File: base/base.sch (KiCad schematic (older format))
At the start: 24 parts, among them J1 FTDI, J2 Barrel_Jack, J3 CONN_01X40, SW1 SW_Push, U1 Z80CPU, U2 27C256, U3 7404, U4 55257, U5 7432, U6 16550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

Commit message: Cleaned up layout
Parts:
- added SW2: POWER, Buttons_Switches_THT:SW_Tactile_SPST_Angled_PTS645Vx31-2LFS, symbol SW_Push
- added unit 4 of U5
- SW1: value SW_Push -> RESET
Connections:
- net +5V: now also C1.1, U5.14 (Vcc); no longer C1.2
- net GND: now also C1.2, U5.7 (Gnd); no longer C1.1
- net IORQ: now also U5.12; no longer U5.9
- net RESET: no longer J3.20 (P20)
- net UART_CE: now also U5.11; no longer U5.8
- net ~RESET~: now also J3.20 (P20)
- net at U5.10: no longer U3.8
- new net: U3.8, U5.13
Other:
- moved on the sheet: C2, C4, J1, J2, U5C, U7

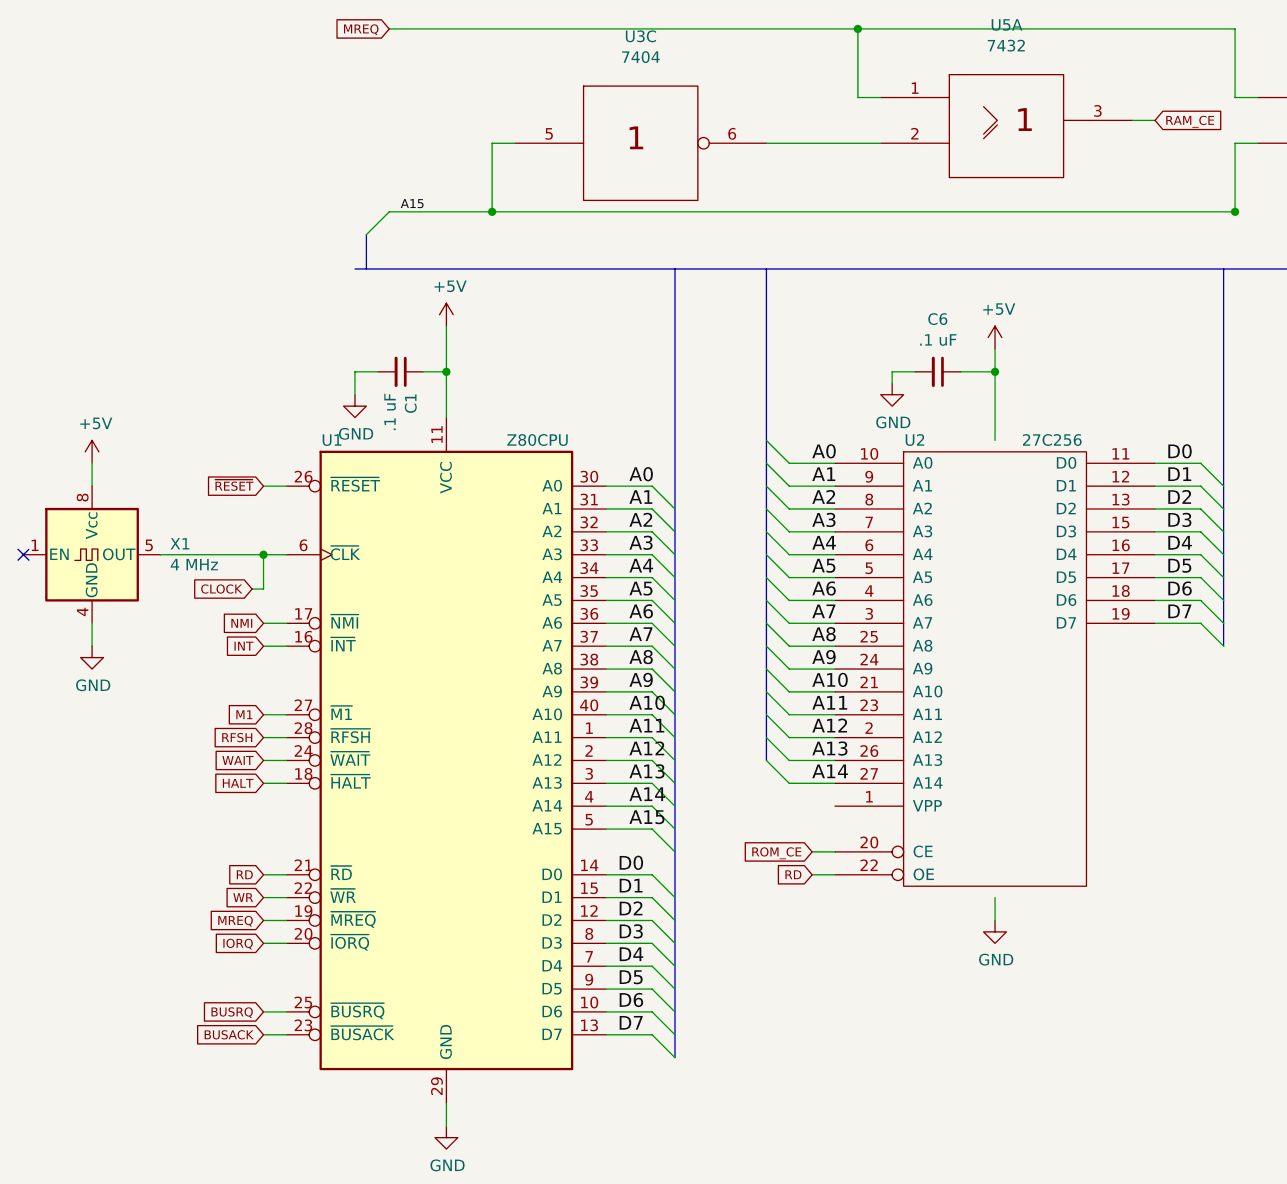
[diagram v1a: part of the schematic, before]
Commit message: Added pullups to busrq and int pins
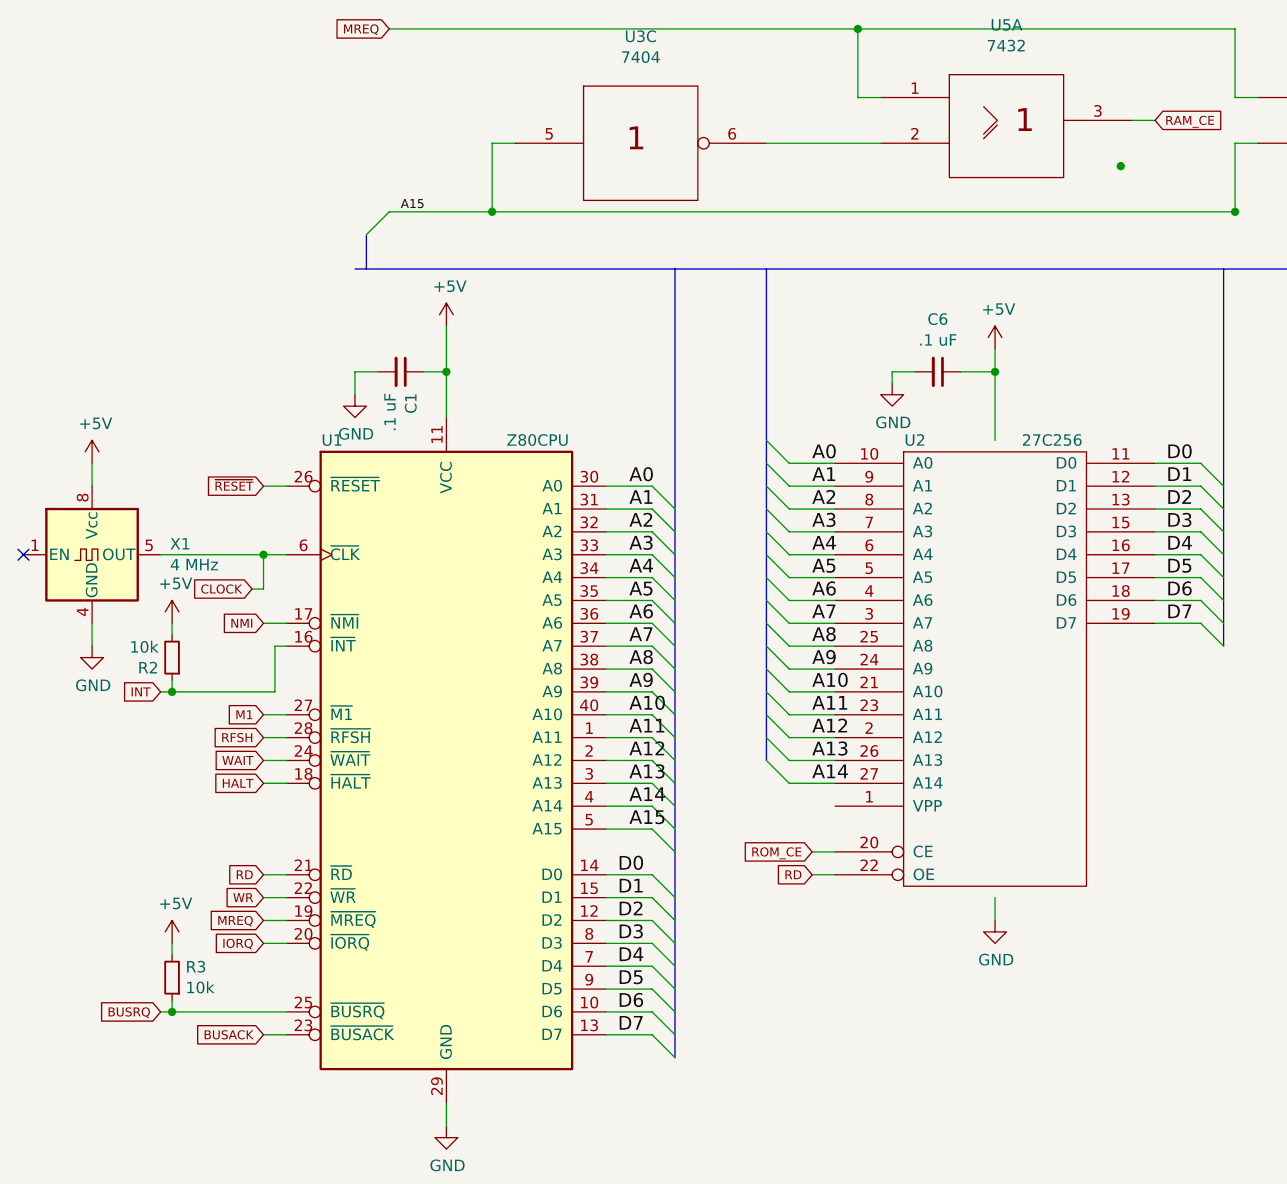
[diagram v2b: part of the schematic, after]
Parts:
- added R2, R3: 10k, Resistors_THT:R_Axial_DIN0207_L6.3mm_D2.5mm_P7.62mm_Horizontal, symbol R_Small
- U5: footprint (none) -> Housings_DIP:DIP-14_W7.62mm_Socket
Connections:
- net +5V: now also R2.2, R3.2
- net BUSRQ: now also R3.1
- net INT: now also R2.1
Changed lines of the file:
@@
 Text GLabel 8950 5400 0    39   Input ~ 0
 INT
-Text GLabel 1700 3400 0    39   Input ~ 0
+Text GLabel 1250 3600 0    39   Input ~ 0
 INT
 Text Label 12500 4100 2    60   ~ 0
@@
 Text GLabel 1700 5100 0    39   Input ~ 0
 BUSACK
-Text GLabel 1700 5000 0    39   Input ~ 0
+Text GLabel 1250 5000 0    39   Input ~ 0
 BUSRQ
 Text GLabel 1700 4000 0    39   Input ~ 0
@@
 	1700 4000 1800 4000
 Wire Wire Line
-	1700 5000 1800 5000
+	1250 5000 1800 5000
 Wire Wire Line
 	1700 5100 1800 5100
@@
 Wire Wire Line
 	12300 2700 12600 2700
-Wire Wire Line
-	1700 3400 1800 3400
 Wire Wire Line
 	8950 5400 9000 5400
@@
 F 0 "U5" H 9500 1616 50  0000 C CNN
 F 1 "7432" H 9500 1525 50  0000 C CNN
-F 2 "" H 9500 1200 60  0001 C CNN
+F 2 "Housings_DIP:DIP-14_W7.62mm_Socket" H 9500 1200 60  0001 C CNN
 F 3 "" H 9500 1200 60  0001 C CNN
 	4    9500 1200
 	1    0    0    -1
 $EndComp
+Connection ~ 5450 1300
+$Comp
+L R_Small R3
+U 1 1 5A8B05D2
+P 1300 4850
+F 0 "R3" H 1241 4804 50  0000 R CNN
+F 1 "10k" H 1241 4895 50  0000 R CNN
+F 2 "Resistors_THT:R_Axial_DIN0207_L6.3mm_D2.5mm_P7.62mm_Horizontal" H 1300 4850 50  0001 C CNN
+F 3 "" H 1300 4850 50  0001 C CNN
+	1    1300 4850
+	-1   0    0    1
+$EndComp
+$Comp
+L +5V #PWR032
+U 1 1 5A8B0B6E
+P 1300 4700
+F 0 "#PWR032" H 1300 4550 50  0001 C CNN
+F 1 "+5V" H 1315 4873 50  0000 C CNN
+F 2 "" H 1300 4700 50  0001 C CNN
+F 3 "" H 1300 4700 50  0001 C CNN
+	1    1300 4700
+	1    0    0    -1
+$EndComp
+Wire Wire Line
+	1300 4700 1300 4750
+Wire Wire Line
+	1300 4950 1300 5000
+Connection ~ 1300 5000
+$Comp
+L +5V #PWR033
+U 1 1 5A8B13B3
+P 1300 3300
+F 0 "#PWR033" H 1300 3150 50  0001 C CNN
+F 1 "+5V" H 1315 3473 50  0000 C CNN
+F 2 "" H 1300 3300 50  0001 C CNN
+F 3 "" H 1300 3300 50  0001 C CNN
+	1    1300 3300
+	1    0    0    -1
+$EndComp
+$Comp
+L R_Small R2
+U 1 1 5A8B151F
+P 1300 3450
+F 0 "R2" H 1359 3496 50  0000 L CNN
+F 1 "10k" H 1359 3405 50  0000 L CNN
+F 2 "Resistors_THT:R_Axial_DIN0207_L6.3mm_D2.5mm_P7.62mm_Horizontal" H 1300 3450 50  0001 C CNN
+F 3 "" H 1300 3450 50  0001 C CNN
+	1    1300 3450
+	-1   0    0    1
+$EndComp
+Wire Wire Line
+	1300 3300 1300 3350
+Wire Wire Line
+	1250 3600 1750 3600
+Wire Wire Line
+	1300 3600 1300 3550
+Wire Wire Line
+	1750 3600 1750 3400
+Wire Wire Line
+	1750 3400 1800 3400
+Connection ~ 1300 3600
 $EndSCHEMATC
